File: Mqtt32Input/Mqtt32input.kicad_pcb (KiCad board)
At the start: 2 copper layers, 97.8 x 81.3 mm, 42 parts, among them J1 INPUT 0-7, J10 SLAVE2 IN/DATA OUTPUT, J2 JP OPT1, J3 JP OPT2, J4 INPUT 8-15, J5 INPUT 16-23, J6 SLAVE1IN/CHAIN INPUT, J7 JP CHAIN IN(1)/SLAVE1(3), J8 JP DATA OUT(1)/SLAVE2(3), J9 INPUT 24-31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

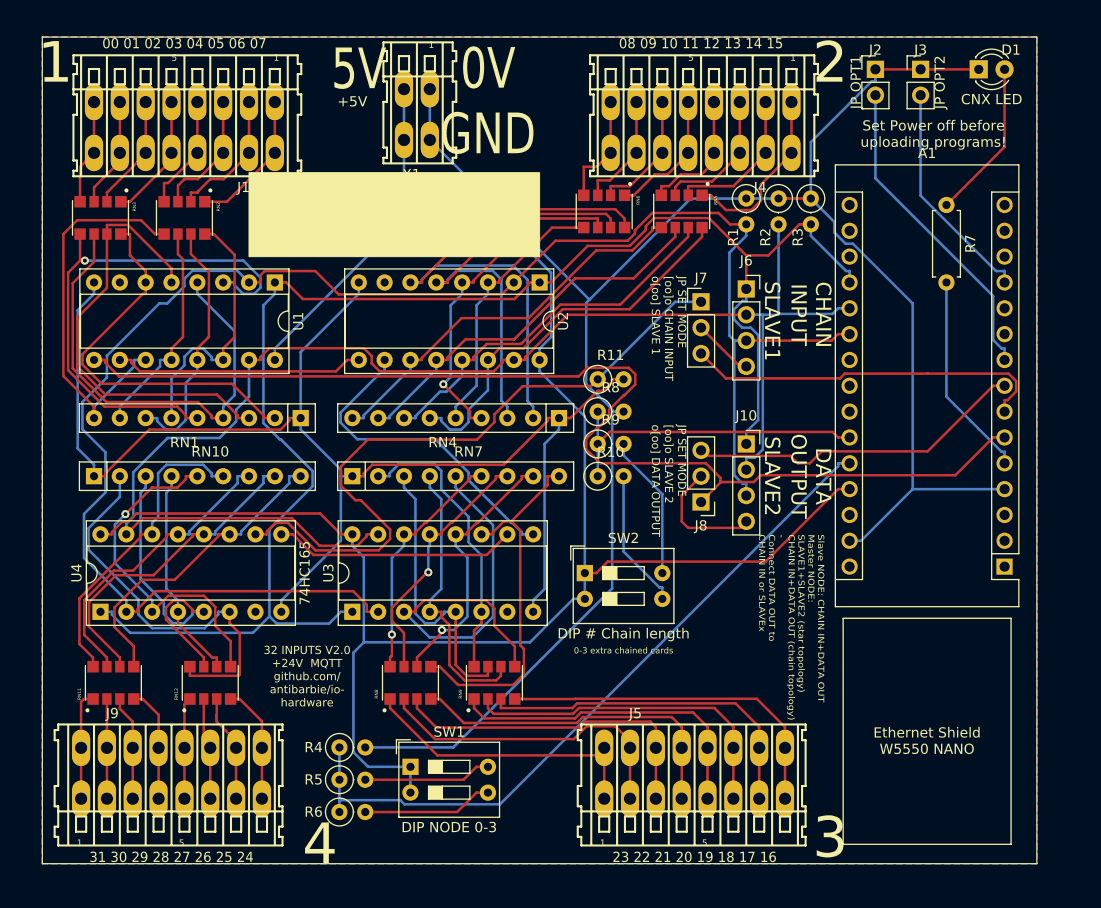
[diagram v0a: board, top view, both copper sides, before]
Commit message: Fix component placement, and GND connexion + board size on inputs
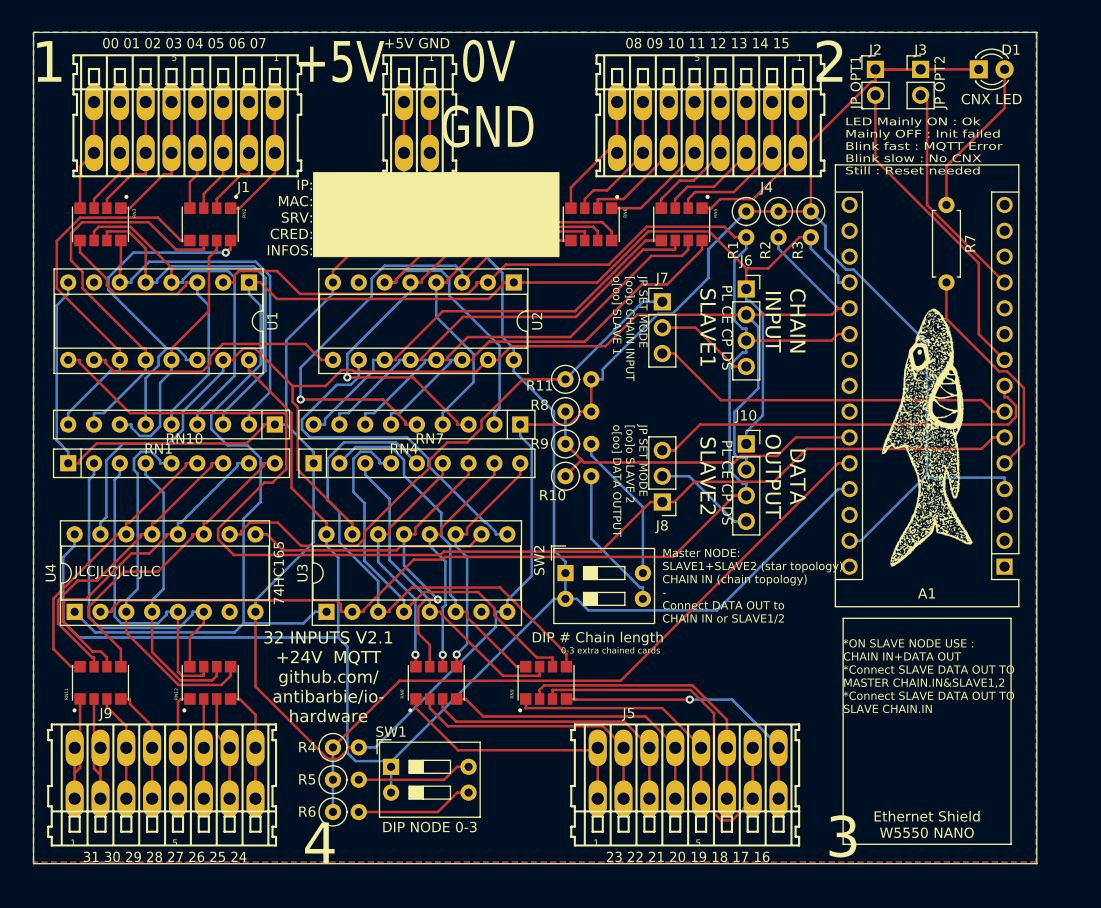
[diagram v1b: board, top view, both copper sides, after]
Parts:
- added G***: LOGO, _Extra_footprints:shark, F.Cu at (189.9, 62.2)
- moved RN9 5.08 mm to (152.4, 86.4)
- moved RN7 4.02 mm to (129.5, 64.8)
- moved RN4 3.86 mm to (149.9, 61.0)
- moved J7 3.81 mm to (163.8, 48.9)
- moved J8 3.81 mm to (163.8, 68.6)
- moved R10 3.17 mm to (154.3, 66.0)
- moved R11 3.17 mm to (154.3, 56.5)
- moved R8 3.17 mm to (154.3, 59.7)
- moved R9 3.17 mm to (154.3, 62.9)
- moved RN10 2.84 mm to (105.4, 64.8)
- moved RN1 2.62 mm to (125.7, 61.0)
- moved RN2 2.62 mm to (119.4, 41.3)
- moved U1 2.54 mm to (123.2, 47.0)
- moved RN8 2.54 mm to (141.6, 86.4)
- moved U2 2.54 mm to (149.2, 47.0)
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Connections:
- R11 pad 2: Net-(R11-Pad2) -> Earth
- RN1 pad 1: Net-(R11-Pad2) -> Earth
- RN10 pad 1: Net-(R11-Pad2) -> Earth
- RN4 pad 1: Net-(R11-Pad2) -> Earth
- RN7 pad 1: Net-(R11-Pad2) -> Earth
- U1 pad 8: Net-(R11-Pad2) -> Earth
- U2 pad 8: Net-(R11-Pad2) -> Earth
- U3 pad 8: Net-(R11-Pad2) -> Earth
- U4 pad 8: Net-(R11-Pad2) -> Earth
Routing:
- net Net-(R11-Pad2): track 134.6 -> 0.00 mm
- net Earth: track 190.8 -> 286.6 mm
- net Net-(RN4-Pad5): track 26.4 -> 50.5 mm, vias 0 -> 1
- net Net-(RN1-Pad5): track 52.7 -> 31.4 mm, vias 1 -> 0
- net Net-(RN1-Pad8): track 21.5 -> 40.2 mm
- net Net-(RN7-Pad4): track 27.7 -> 41.1 mm
- net Net-(RN7-Pad9): track 36.5 -> 24.2 mm, vias 0 -> 1
- net Net-(J7-Pad1): track 67.5 -> 55.4 mm
- net Net-(RN1-Pad4): track 46.3 -> 34.9 mm
- net Net-(RN1-Pad6): track 25.9 -> 35.4 mm, vias 0 -> 1
- net Net-(A1-Pad6): track 113.0 -> 122.1 mm
- net Net-(RN7-Pad5): track 42.4 -> 51.0 mm
- net Net-(J5-PadA5): track 32.2 -> 24.8 mm
- net Net-(RN10-Pad4): track 21.3 -> 28.3 mm
- net Net-(J5-PadA8): track 34.8 -> 27.9 mm, vias 0 -> 1
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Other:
- board size 97.8 x 81.3 mm -> 98.7 x 81.7 mm
- board text added: "*ON SLAVE NODE USE : CHAIN IN+DATA OUT *Connect SLAVE DATA OUT TO MASTER CHAIN.IN&SLAVE1,2 *Connect SLAVE DATA OUT TO SLAVE CHAIN.IN"
- board text added: "+5V GND"
- board text added: "32 INPUTS V2.1 +24V MQTT github.com/ antibarbie/io- hardware"
- board text added: "IP: MAC: SRV: CRED: INFOS:"
- board text added: "JLCJLCJLCJLC"
- board text added: "LED Mainly ON : Ok Mainly OFF : Init failed Blink fast : MQTT Error Blink slow : No CNX Still : Reset needed"
- board text added: "Master NODE: SLAVE1+SLAVE2 (star topology) CHAIN IN (chain topology) - Connect DATA OUT to CHAIN IN or SLAVE1/2"
- board text added: "PL CE CP DS"
- board text removed: "32 INPUTS V2.0 +24V MQTT github.com/ antibarbie/io- hardware"
- board text removed: "5V"
- board text removed: "Set Power off before uploading programs!"
- board text removed: "Slave NODE: CHAIN IN+DATA OUT Master NODE: SLAVE1+SLAVE2 (star topology) CHAIN IN+DATA OUT (chain topology) - Connect DATA OUT to CHAIN IN or SLAVEx"

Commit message: Revision with through hole resistor, more robust that SMD Array
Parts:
- removed G***: LOGO, _Extra_footprints:shark
- removed RN11, RN12, RN2, RN3, RN5, RN6, RN8, RN9: 47k, _Extra_footprints:RESCAXS127P508X320X70-8N
- added RIN1: 47k, Resistor_THT:R_Axial_DIN0207_L6.3mm_D2.5mm_P2.54mm_Vertical, F.Cu at (125.8, 39.6)
- added RIN10: 47k, Resistor_THT:R_Axial_DIN0207_L6.3mm_D2.5mm_P2.54mm_Vertical, F.Cu at (175.4, 39.0)
- added RIN11: 47k, Resistor_THT:R_Axial_DIN0207_L6.3mm_D2.5mm_P2.54mm_Vertical, F.Cu at (172.4, 39.0)
- added RIN12: 47k, Resistor_THT:R_Axial_DIN0207_L6.3mm_D2.5mm_P2.54mm_Vertical, F.Cu at (169.4, 39.0)
- added RIN13: 47k, Resistor_THT:R_Axial_DIN0207_L6.3mm_D2.5mm_P2.54mm_Vertical, F.Cu at (166.4, 39.0)
- added RIN14: 47k, Resistor_THT:R_Axial_DIN0207_L6.3mm_D2.5mm_P2.54mm_Vertical, F.Cu at (163.4, 39.0)
- added RIN15: 47k, Resistor_THT:R_Axial_DIN0207_L6.3mm_D2.5mm_P2.54mm_Vertical, F.Cu at (160.4, 39.0)
- added RIN16: 47k, Resistor_THT:R_Axial_DIN0207_L6.3mm_D2.5mm_P2.54mm_Vertical, F.Cu at (157.4, 39.0)
- added RIN17: 47k, Resistor_THT:R_Axial_DIN0207_L6.3mm_D2.5mm_P2.54mm_Vertical, F.Cu at (156.0, 88.2)
- added RIN18: 47k, Resistor_THT:R_Axial_DIN0207_L6.3mm_D2.5mm_P2.54mm_Vertical, F.Cu at (159.0, 88.2)
- added RIN19: 47k, Resistor_THT:R_Axial_DIN0207_L6.3mm_D2.5mm_P2.54mm_Vertical, F.Cu at (162.0, 88.2)
- added RIN2: 47k, Resistor_THT:R_Axial_DIN0207_L6.3mm_D2.5mm_P2.54mm_Vertical, F.Cu at (122.8, 39.6)
- added RIN20: 47k, Resistor_THT:R_Axial_DIN0207_L6.3mm_D2.5mm_P2.54mm_Vertical, F.Cu at (165.0, 88.2)
- added RIN21: 47k, Resistor_THT:R_Axial_DIN0207_L6.3mm_D2.5mm_P2.54mm_Vertical, F.Cu at (168.0, 88.2)
- added RIN22: 47k, Resistor_THT:R_Axial_DIN0207_L6.3mm_D2.5mm_P2.54mm_Vertical, F.Cu at (171.0, 88.2)
- added RIN23: 47k, Resistor_THT:R_Axial_DIN0207_L6.3mm_D2.5mm_P2.54mm_Vertical, F.Cu at (174.0, 88.2)
- added RIN24: 47k, Resistor_THT:R_Axial_DIN0207_L6.3mm_D2.5mm_P2.54mm_Vertical, F.Cu at (177.0, 88.2)
- added RIN25: 47k, Resistor_THT:R_Axial_DIN0207_L6.3mm_D2.5mm_P2.54mm_Vertical, F.Cu at (104.8, 88.0)
- added RIN26: 47k, Resistor_THT:R_Axial_DIN0207_L6.3mm_D2.5mm_P2.54mm_Vertical, F.Cu at (107.8, 88.0)
- added RIN27: 47k, Resistor_THT:R_Axial_DIN0207_L6.3mm_D2.5mm_P2.54mm_Vertical, F.Cu at (110.8, 88.0)
- added RIN28: 47k, Resistor_THT:R_Axial_DIN0207_L6.3mm_D2.5mm_P2.54mm_Vertical, F.Cu at (113.8, 88.0)
- added RIN29: 47k, Resistor_THT:R_Axial_DIN0207_L6.3mm_D2.5mm_P2.54mm_Vertical, F.Cu at (116.8, 88.0)
- added RIN3: 47k, Resistor_THT:R_Axial_DIN0207_L6.3mm_D2.5mm_P2.54mm_Vertical, F.Cu at (119.8, 39.6)
- added RIN30: 47k, Resistor_THT:R_Axial_DIN0207_L6.3mm_D2.5mm_P2.54mm_Vertical, F.Cu at (119.8, 88.0)
- added RIN31: 47k, Resistor_THT:R_Axial_DIN0207_L6.3mm_D2.5mm_P2.54mm_Vertical, F.Cu at (122.8, 88.0)
- added RIN32: 47k, Resistor_THT:R_Axial_DIN0207_L6.3mm_D2.5mm_P2.54mm_Vertical, F.Cu at (125.8, 88.0)
- added RIN4: 47k, Resistor_THT:R_Axial_DIN0207_L6.3mm_D2.5mm_P2.54mm_Vertical, F.Cu at (116.8, 39.6)
- added RIN5: 47k, Resistor_THT:R_Axial_DIN0207_L6.3mm_D2.5mm_P2.54mm_Vertical, F.Cu at (113.8, 39.6)
- added RIN6: 47k, Resistor_THT:R_Axial_DIN0207_L6.3mm_D2.5mm_P2.54mm_Vertical, F.Cu at (110.8, 39.6)
- added RIN7: 47k, Resistor_THT:R_Axial_DIN0207_L6.3mm_D2.5mm_P2.54mm_Vertical, F.Cu at (107.8, 39.6)
- added RIN8: 47k, Resistor_THT:R_Axial_DIN0207_L6.3mm_D2.5mm_P2.54mm_Vertical, F.Cu at (104.8, 39.6)
- added RIN9: 47k, Resistor_THT:R_Axial_DIN0207_L6.3mm_D2.5mm_P2.54mm_Vertical, F.Cu at (178.4, 39.0)
- moved R3 25.3 mm to (153.8, 46.0), turned to 0 degrees
- moved R2 23.3 mm to (153.8, 49.1), turned to 0 degrees
- moved R1 22.0 mm to (153.8, 52.3), turned to 0 degrees
- moved J1 0.25 mm to (116.8, 32.0)
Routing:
- net Net-(RIN10-Pad2): track 42.0 -> 108.5 mm
- net Net-(RIN9-Pad2): track 42.8 -> 85.9 mm
- net Net-(RIN24-Pad2): track 34.0 -> 73.8 mm
- net Net-(RIN18-Pad2): track 24.0 -> 58.3 mm, vias 1 -> 0
- net Net-(RIN20-Pad2): track 24.8 -> 56.2 mm, vias 1 -> 0
- net Net-(J5-PadA7): track 37.6 -> 10.1 mm
- net Net-(A1-Pad6): track 122.1 -> 149.5 mm
- net Net-(RIN23-Pad2): track 31.7 -> 59.0 mm
- net Net-(RIN32-Pad2): track 33.8 -> 57.5 mm
- net /PL: track 153.4 -> 177.0 mm
- net Net-(RIN19-Pad2): track 26.6 -> 49.6 mm, vias 1 -> 0
- net Net-(RIN11-Pad2): track 40.7 -> 60.6 mm
- net Net-(J5-PadA4): track 28.6 -> 9.59 mm
- net Net-(J5-PadA6): track 28.7 -> 9.89 mm
- net Net-(J5-PadA3): track 27.9 -> 9.78 mm
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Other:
- board text added: "32 INPUTS V2.2 +24V MQTT github.com/ antibarbie/io- hardware"
- board text added: "SLAVE NODE: USE CHAIN IN+DATA OUT *Connect SLAVE DATA OUT TO MASTER CHAIN.IN&SLAVE1,2 *Connect SLAVE DATA OUT TO SLAVE CHAIN.IN"
- board text removed: "*ON SLAVE NODE USE : CHAIN IN+DATA OUT *Connect SLAVE DATA OUT TO MASTER CHAIN.IN&SLAVE1,2 *Connect SLAVE DATA OUT TO SLAVE CHAIN.IN"
- board text removed: "32 INPUTS V2.1 +24V MQTT github.com/ antibarbie/io- hardware"
